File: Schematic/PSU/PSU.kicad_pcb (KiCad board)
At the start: 2 copper layers, 71 x 39 mm, 11 parts, among them J1 Conn_01x02, J3 Mains in, SW1 SW_SPDT

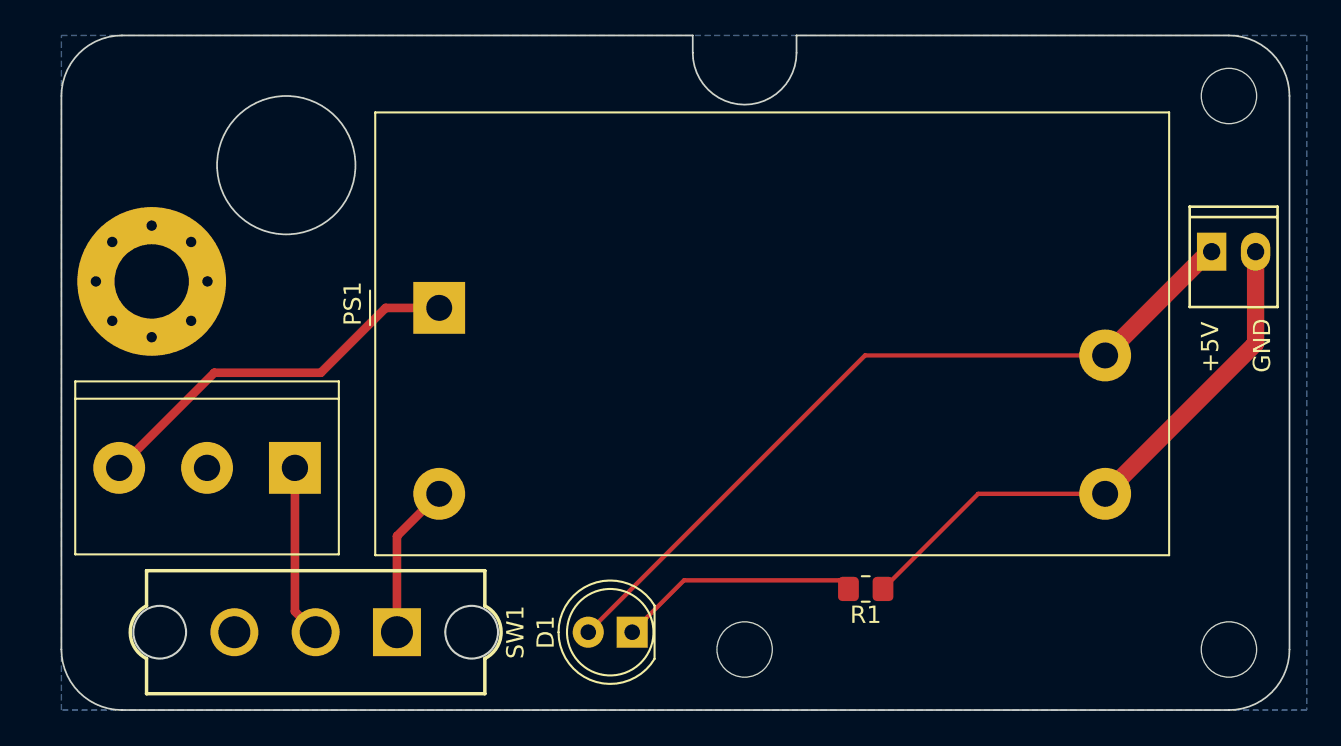
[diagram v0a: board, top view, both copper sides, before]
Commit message: Adjusted mounting hole position
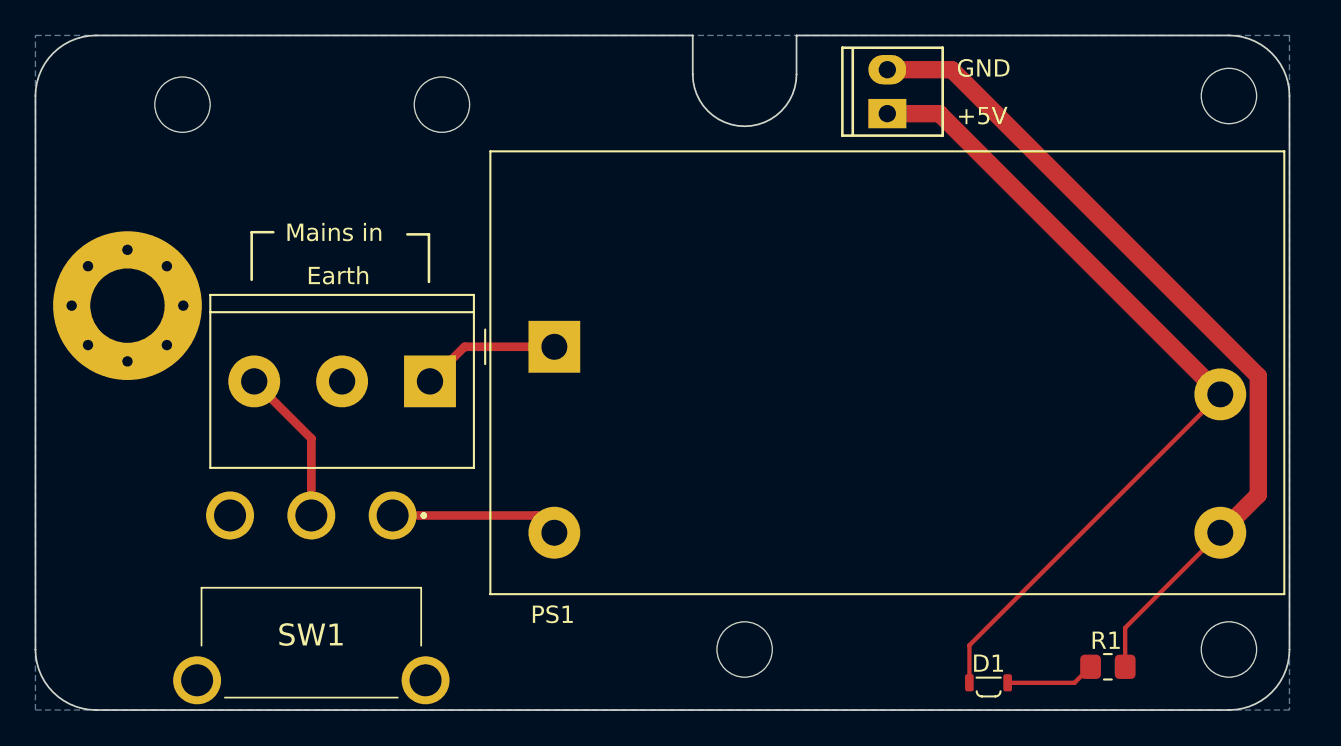
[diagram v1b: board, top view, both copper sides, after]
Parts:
- added H5: MountingHole, MountingHole:MountingHole_3.2mm_M3, F.Cu at (120.0, 70.0)
- added H6: MountingHole, MountingHole:MountingHole_3.2mm_M3, F.Cu at (135.0, 70.0)
- D1: footprint LED_THT:LED_D5.0mm -> myDevices:LED_Everlight_Side_1x2.1mm
- SW1: footprint myDevices:1101M1S3CQE2 -> myDevices:1101M2S3ABE2
- moved J1 22.1 mm to (160.8, 69.2), turned to 90 degrees
- moved D1 21.9 mm to (167.7, 103.4)
- moved G*** 16.5 mm to (160.0, 83.2)
- moved R1 14.7 mm to (173.5, 102.5)
- moved J2 9.27 mm to (134.3, 86.0)
- moved PS1 7.03 mm to (141.5, 84.0)
- moved SW1 6.75 mm to (132.2, 93.8), turned to 0 degrees
- moved H1 1.98 mm to (116.8, 81.6)
- renumbered H5 to H1, H1 to H2, H2 to H3, H3 to H4, J3 to J2
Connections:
- J2 pad 1: Net-(J3-Pin_1) -> Net-(J2-Pin_1)
- J2 pad 3: Net-(J3-Pin_3) -> Net-(J2-Pin_3)
- PS1 pad 1: Net-(J3-Pin_3) -> Net-(J2-Pin_1)
- SW1 pad 2: Net-(J3-Pin_1) -> Net-(J2-Pin_3)
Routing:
- net Net-(J3-Pin_3): track 22.3 -> 0.00 mm
- net GND: track 32.7 -> 48.8 mm
- net Net-(J3-Pin_1): track 10.00 -> 0.00 mm
- net Net-(J2-Pin_3): track 0.00 -> 9.12 mm
- net Net-(D1-K): track 13.9 -> 5.18 mm
- net Net-(J2-Pin_1): track 0.00 -> 8.02 mm
- net +5V: track 43.8 -> 48.7 mm
- net Net-(PS1-AC/L): track 9.01 -> 9.76 mm
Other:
- board size 71 x 39 mm -> 72.5 x 39 mm
- board text added: "Andonstar_PSU R0142B_2331 Bjørner Sandom"
- board text added: "Earth"
- board text added: "Mains in"
- board text removed: "Andonstar_PSU R0142_2329 Bjørner Sandom"

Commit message: Updated production files
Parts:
- J1: value Conn_01x02 -> 5V output; footprint myDevices:KF2510-2P -> Connector_Molex:Molex_KK-254_AE-6410-02A_1x02_P2.54mm_Vertical
- J2: footprint myDevices:TerminalBlock_LCSC_P5.08mm_3 -> Retronics_Connectors:ScrewTerminal_DB128L-5.08-3P-BK-S
- moved J1 1.21 mm to (160.8, 70.5)
